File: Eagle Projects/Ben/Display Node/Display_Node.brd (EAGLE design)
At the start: 100 x 80 mm, 28 parts, among them Q1 16MHz, Q3 16MHz, Q4 16MHz, U1 ATMEGA328P_TQFP, U2 MCP2551

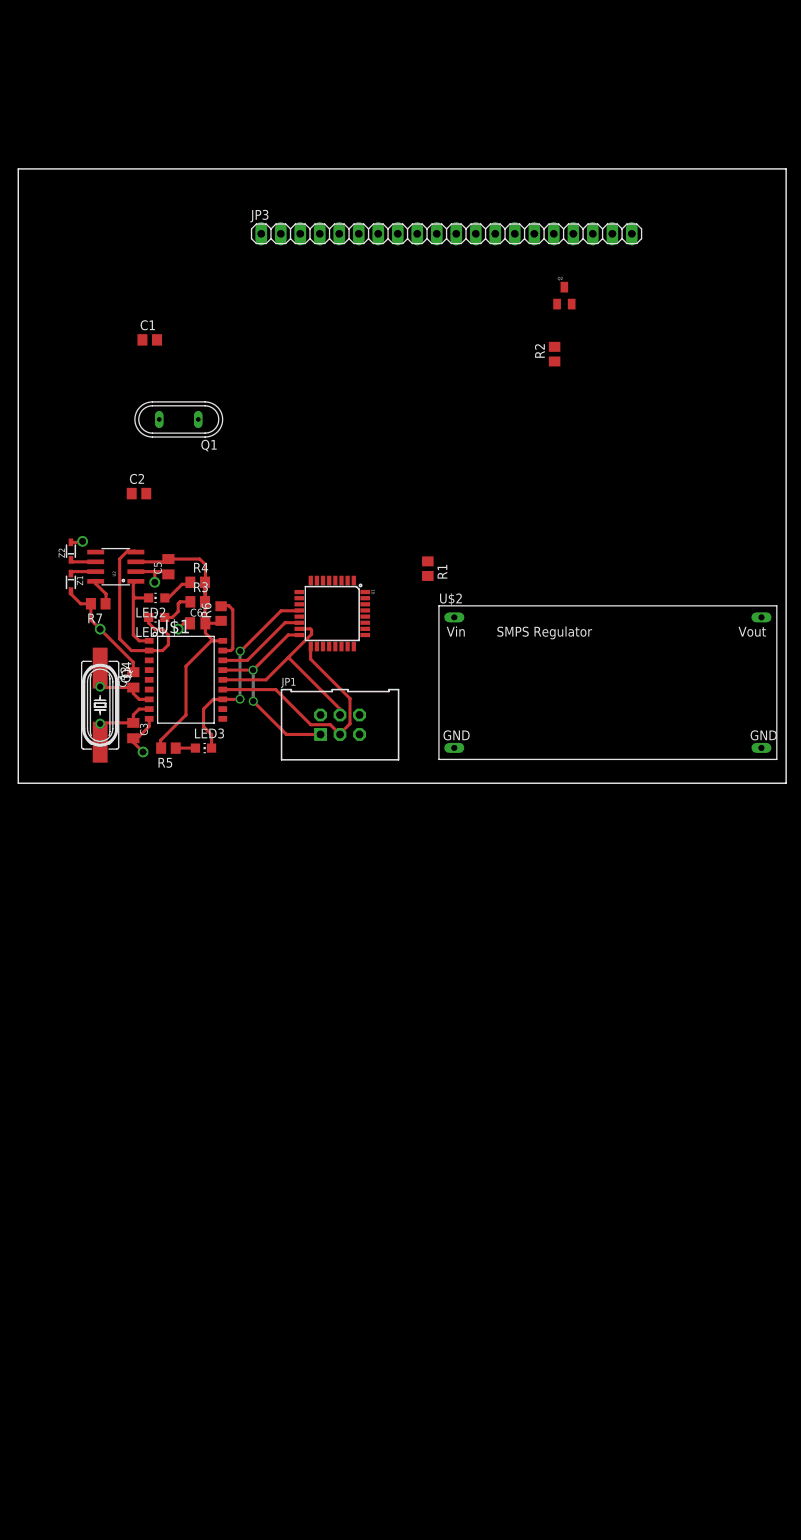
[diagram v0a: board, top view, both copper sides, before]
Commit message: Small change to library pin display
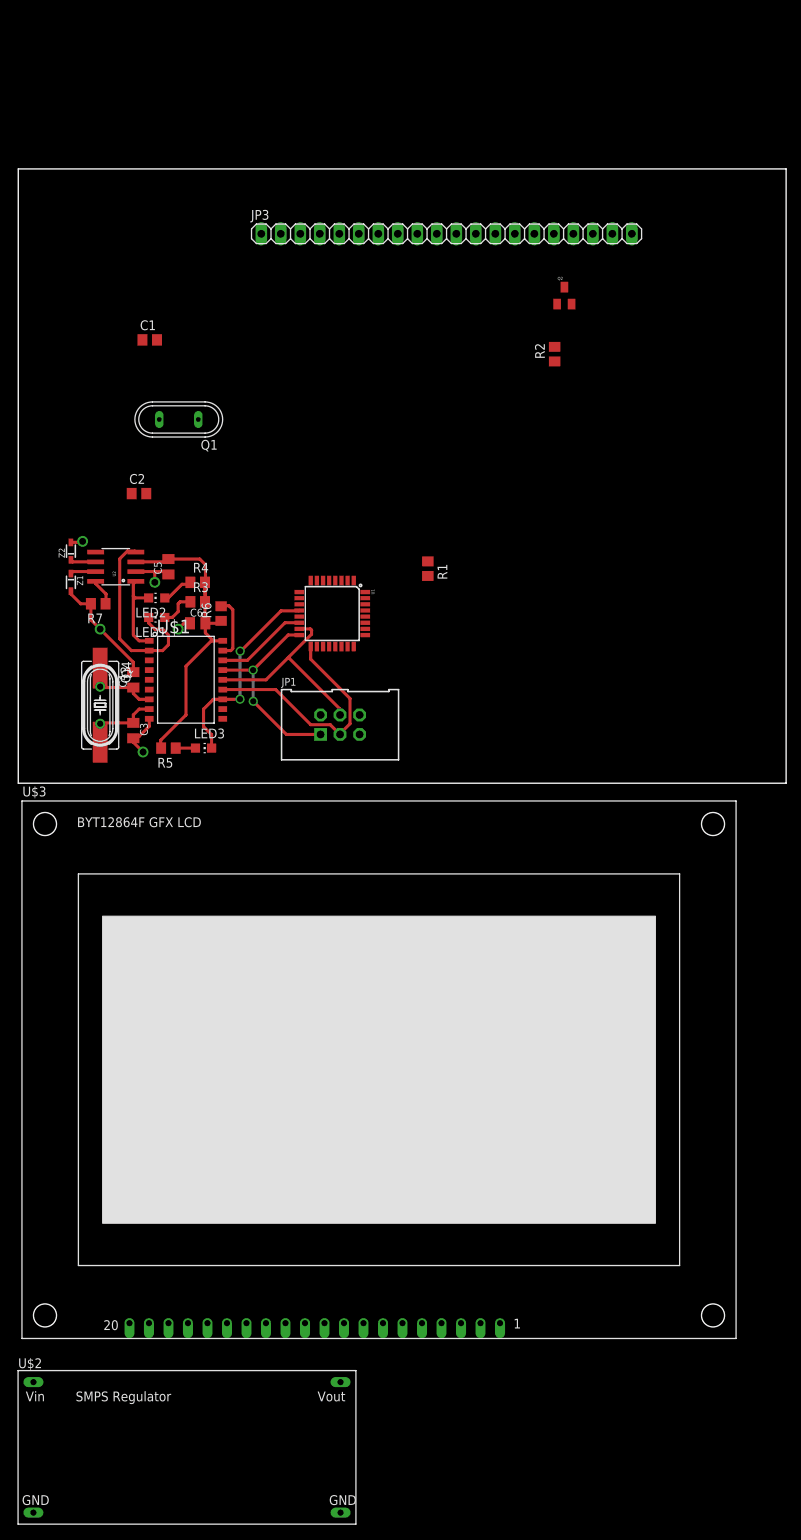
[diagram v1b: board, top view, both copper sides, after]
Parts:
- added U$3: BYT12864FLCD, RobThePyro:BYT12864F
- moved U$2 113.7 mm to (-0.03, -96.5)
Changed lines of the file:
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@@
 <element name="Z1" library="supressor" package="SOD323" value="TVS-UD-SOD323" x="6.858" y="26.162" rot="R270"/>
 <element name="Z2" library="supressor" package="SOD323" value="TVS-UD-SOD323" x="6.858" y="30.226" rot="R90"/>
-<element name="U$2" library="RobThePyro" package="SMPSBOARD" value="SMPSBOARD" x="54.7878" y="3.0988"/>
+<element name="U$3" library="RobThePyro" package="BYT12864F" value="BYT12864FLCD" x="0.4826" y="-72.3138"/>
+<element name="U$2" library="RobThePyro" package="SMPSBOARD" value="SMPSBOARD" x="-0.0254" y="-96.4946"/>
 </elements>
 <signals>

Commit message: Workin on stuff...
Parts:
- removed JP3: GFX_LCD, adafruit:1X20
- added X1, X2: 5566-6, con-molex:5566-6
- moved U$3 176.9 mm to (94.5, 77.6), turned to 180 degrees
- moved U$2 155.3 mm to (21.7, 57.3)
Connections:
- new net +12V: U$2.VIN, X1.1, X2.1
- new net LCD_RST: U$3.P$4
- new net N$14: X1.5, X2.5
- new net N$15: X1.6, X2.6
- net +5V: now also U$2.VOUT, U$3.P$19, U$3.P$2; no longer JP3.17, JP3.19, JP3.2
- net CANH: now also X1.3, X2.3
- net CANL: now also X1.4, X2.4
- net GND: now also U$2.GND, U$2.GND@, U$3.P$20, U$3.P$6, X1.2, X2.2; no longer JP3.1, JP3.15
- net LCD_CS: now also U$3.P$17; no longer JP3.4
- net MOSI: now also U$3.P$16; no longer JP3.5
- net N$4: now also U$3.P$1; no longer JP3.20
- net SCK: now also U$3.P$15; no longer JP3.6

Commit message: Almost lost some important stuff! managed to save it :D
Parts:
- added JP2: (no value), pinhead:1X02
- added Q5: 16MHz, crystal:HC49UP
- moved U$3 71.6 mm to (93.0, 6.00)
- moved Q2 45.6 mm to (35.9, 34.6)
- moved R2 38.5 mm to (39.9, 31.6), turned to 180 degrees
- moved C1 35.7 mm to (50.7, 45.6), turned to 270 degrees
- moved C2 33.2 mm to (48.0, 45.6), turned to 270 degrees
- moved X2 32.4 mm to (9.91, 49.7)
- moved Q1 29.4 mm to (49.4, 40.3)
- moved U$2 26.0 mm to (17.1, 82.8), turned to 270 degrees
- moved U1 13.0 mm to (51.8, 29.1)
- moved X1 9.05 mm to (9.91, 70.8)
- moved R1 8.65 mm to (57.4, 35.6), turned to 180 degrees
- moved C5 7.00 mm to (19.6, 35.2)
- moved U2 7.00 mm to (12.7, 35.2)
- moved C3 7.00 mm to (15.0, 13.9)
- moved C4 7.00 mm to (15.0, 20.5)
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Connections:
- new net N$10: JP1.2, JP2.2
- net +12V: now also X1.3, X2.3; no longer X1.1, X2.1
- net +5V: now also JP2.1; no longer JP1.2
- net CANH: now also X1.1, X2.1; no longer X1.3, X2.3
- net N$1: now also Q5.2
- net N$2: now also Q5.1
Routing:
- net +12V: track 0.00 -> 60.7 mm
- net +5V: track 44.2 -> 90.3 mm
- net CANH: track 3.33 -> 42.5 mm
- net CANL: track 3.33 -> 41.4 mm
- net N$15: track 0.00 -> 23.4 mm
- net N$14: track 0.00 -> 23.2 mm
- net N$1: track 0.00 -> 12.7 mm
- net N$2: track 0.00 -> 12.7 mm
- net MISO: track 26.5 -> 37.6 mm
- net CANCS: track 12.0 -> 22.9 mm
- net CANINT: track 27.1 -> 38.1 mm
- net MOSI: track 26.5 -> 31.7 mm
- net GND: track 29.6 -> 32.3 mm
- net SCK: track 31.8 -> 33.8 mm
- added copper zone on layer 16, net GND
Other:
- board size 100 x 80 mm -> 100 x 100 mm

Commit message: Moar Layout on display
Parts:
- removed Q2: (no value), SparkFun:SOT23
- added Q6, Q7: 2N7002, transistor-fet:SOT23
- added R8: 100E, resistor:R0805
- R2: value 1k -> 100E
- moved R2 35.6 mm to (67.9, 9.67)
- moved R1 7.15 mm to (61.1, 29.4), turned to 0 degrees
- moved JP2 2.45 mm to (30.7, 12.1), turned to 90 degrees
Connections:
- new net N$11: Q6.2, U$3.P$15
- new net N$12: Q6.1, R8.2
- new net N$13: U1.1
- new net N$16: U1.32
- new net N$17: U1.30
- new net N$18: U1.31
- new net SCKCNTRL: R8.1, U1.10
- net GND: now also Q7.2; no longer Q2.2
- net N$4: now also Q7.3; no longer Q2.3
- net N$5: now also Q7.1; no longer Q2.1
- net SCK: now also Q6.3; no longer U$3.P$15
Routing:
- net +5V: track 90.3 -> 203.4 mm
- net LCD_CS: track 0.00 -> 39.0 mm, vias 0 -> 2
- net LCD_PWM: track 0.00 -> 37.2 mm, vias 0 -> 2
- net GND: track 32.3 -> 60.5 mm, vias 5 -> 7
- net N$12: track 0.00 -> 27.7 mm, vias 0 -> 2
- net N$10: track 0.00 -> 13.3 mm
- net MOSI: track 31.7 -> 44.2 mm
- net SCKCNTRL: track 0.00 -> 8.02 mm
- net N$4: track 0.00 -> 6.68 mm
- net SCK: track 33.8 -> 40.0 mm
- net N$5: track 0.00 -> 4.53 mm
- net N$11: track 0.00 -> 3.72 mm
- net MISO: track 37.6 -> 35.9 mm

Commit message: Birds Tweeting. Shit. Bed Time..
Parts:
- added LED4, LED5: (no value), led:CHIP-LED0805
- added R10, R9: 1k, resistor:R0805
- added S1: RESET, SparkFun:TACTILE_SWITCH_SMD
- added X3: C-GRID-10-70553, con-molex:70553-10
- added X4: C-GRID-06-70553, con-molex:70553-06
- moved R1 15.3 mm to (52.1, 17.0), turned to 90 degrees
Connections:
- removed net N$17: U1.30
- removed net N$18: U1.31
- new net A0: U1.27, X3.5
- new net A1: U1.28, X3.6
- new net BTN1: U1.32, X3.1
- new net BTN2: U1.1, X3.2
- new net BTN3: U1.2, X3.3
- new net BTN4: U1.9, X3.4
- new net CRUISE1: U1.23, X4.1
- new net CRUISE2: U1.24, X4.2
- new net CRUISE3: U1.25, X4.3
- new net CRUISE4: U1.26, X4.4
- new net LED1: LED4.C, U1.30, X3.7
- new net LED2: LED5.C, U1.31, X3.8
- new net N$23: X4.5
- new net N$24: X4.6
- net +5V: now also R10.1, R9.1, X3.9
- net GND: now also S1.3, S1.4, X3.10
- net N$13: now also LED4.A, R9.2; no longer U1.1
- net N$16: now also LED5.A, R10.2; no longer U1.32
- net RST: now also S1.1, S1.2
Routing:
- net RST: track 0.00 -> 43.2 mm, vias 0 -> 2
- net BTN4: track 0.00 -> 42.1 mm, vias 0 -> 2
- net LED1: track 0.00 -> 29.7 mm
- net BTN3: track 0.00 -> 29.3 mm
- net LED2: track 0.00 -> 29.2 mm
- net BTN2: track 0.00 -> 28.6 mm
- net BTN1: track 0.00 -> 28.3 mm
- net A0: track 0.00 -> 28.0 mm
- net CRUISE1: track 0.00 -> 24.8 mm
- net CRUISE2: track 0.00 -> 22.5 mm
- net CRUISE3: track 0.00 -> 22.1 mm
- net CRUISE4: track 0.00 -> 21.9 mm
- net GND: track 60.5 -> 77.3 mm
- net A1: track 0.00 -> 7.18 mm
- net +5V: track 203.4 -> 209.4 mm

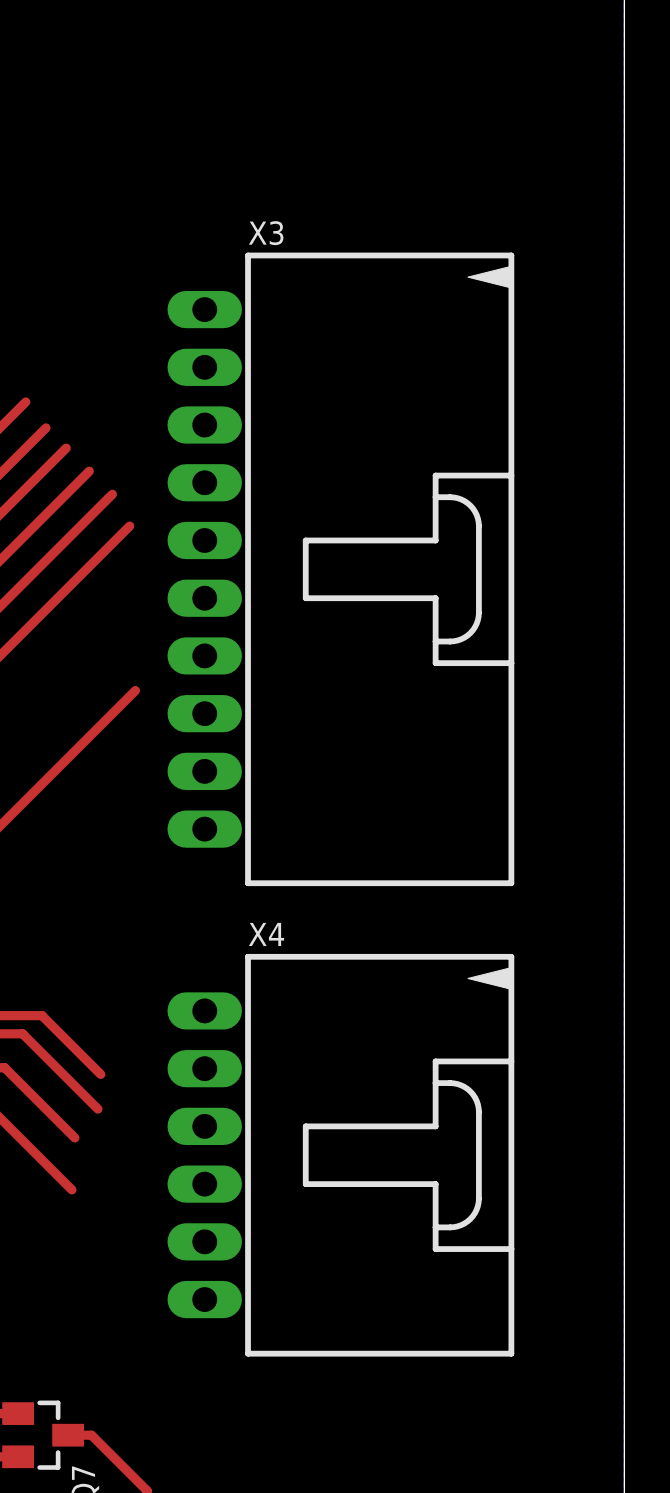
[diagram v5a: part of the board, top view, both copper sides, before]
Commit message: Added homebrew TE Connectivity EP 2.5mm TPA Connector series. Only right angle for now..
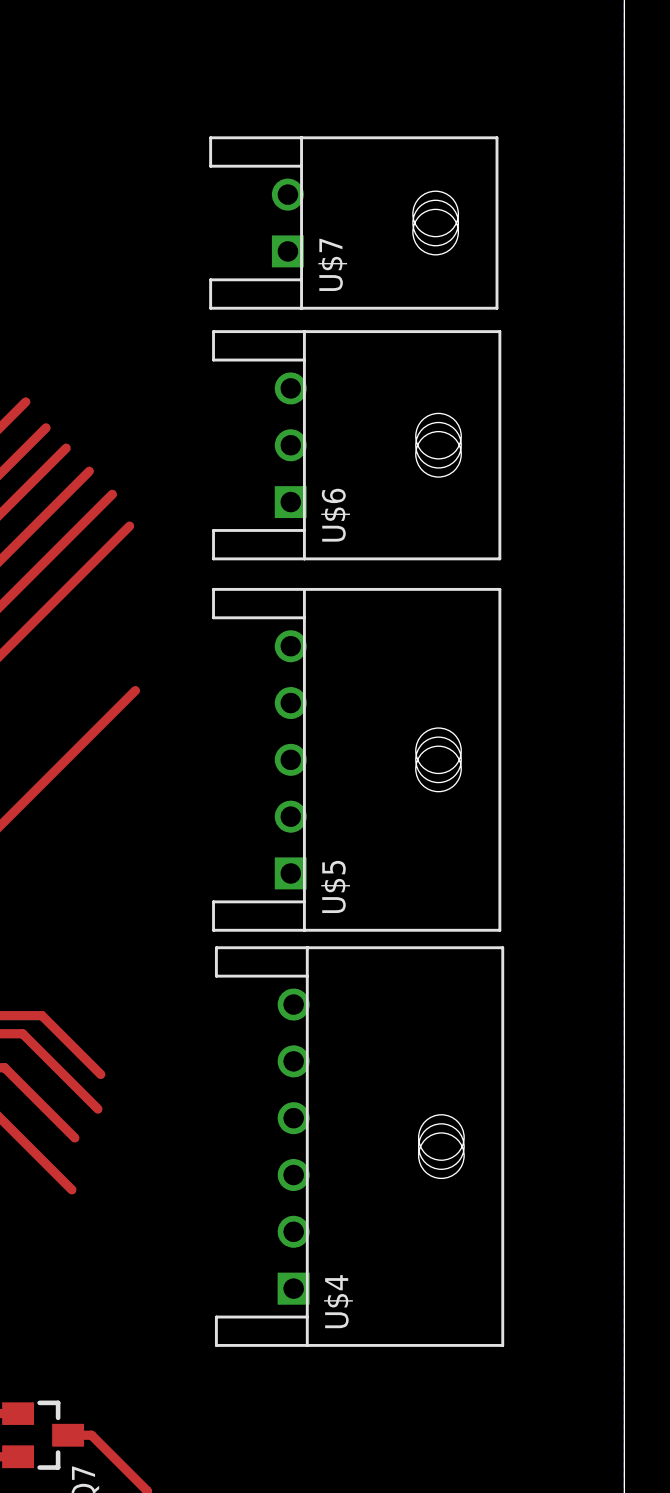
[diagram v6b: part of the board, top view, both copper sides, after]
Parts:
- removed X3: C-GRID-10-70553, con-molex:70553-10
- removed X4: C-GRID-06-70553, con-molex:70553-06
- added U$4: HEADER-6WAY, con-TE-EP:1744426-6
- added U$5: HEADER-5WAY, con-TE-EP:1744426-5
- added U$6: HEADER-3WAY, con-TE-EP:1744426-3
- added U$7: HEADER-2WAY, con-TE-EP:1744426-2
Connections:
- net +5V: no longer X3.9
- net A0: no longer X3.5
- net A1: no longer X3.6
- net BTN1: no longer X3.1
- net BTN2: no longer X3.2
- net BTN3: no longer X3.3
- net BTN4: no longer X3.4
- net CRUISE1: now also U$4.P$6; no longer X4.1
- net CRUISE2: now also U$4.P$5; no longer X4.2
- net CRUISE3: now also U$4.P$4; no longer X4.3
- net CRUISE4: now also U$4.P$3; no longer X4.4
- net GND: no longer X3.10
- net LED1: no longer X3.7
- net LED2: no longer X3.8
- net N$23: now also U$4.P$2; no longer X4.5
- net N$24: now also U$4.P$1; no longer X4.6
